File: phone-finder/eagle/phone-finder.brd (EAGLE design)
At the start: 50 x 50 mm, 45 parts, among them J1 MICRO USB, J2 PHONE-JACK, K1 RELAY, Q1 DTA114EET1G (2x10K), Q2 2N2222, Q3 2N2222, T1 TRANSFORMER, U1 AP2114H-3.3TRG1, U2 NUF2042XV6T1G, U3 LPC11U35FHI33/501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

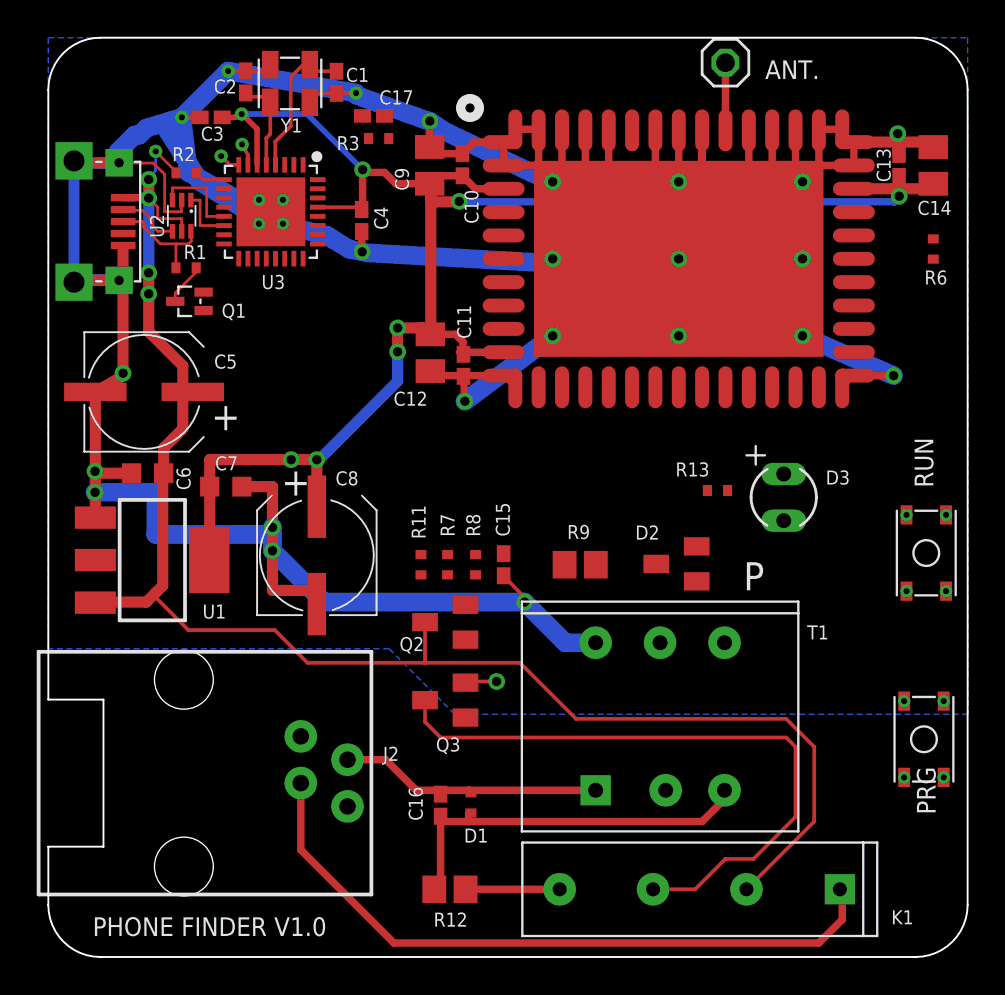
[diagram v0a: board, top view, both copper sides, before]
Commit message: Moved the USB connector 1mm away from the board edge.
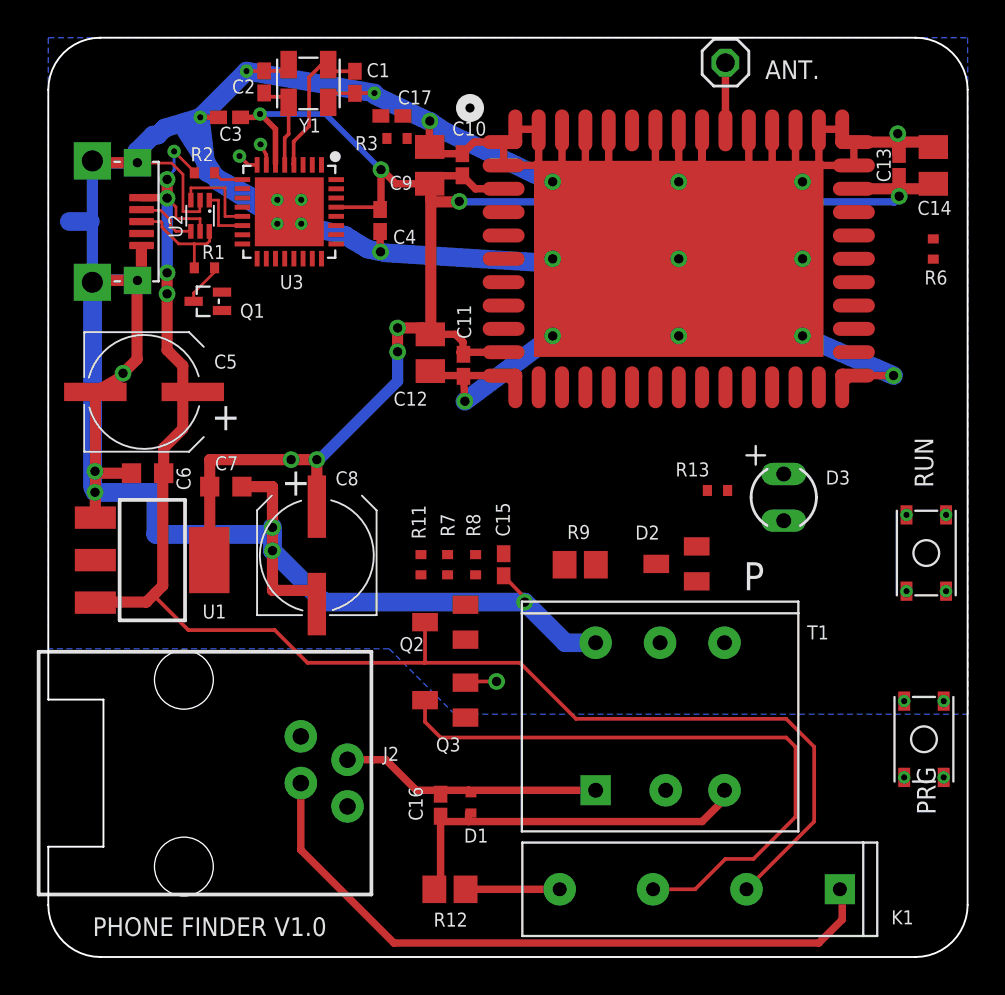
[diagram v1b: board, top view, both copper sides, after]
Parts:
- moved C1 1.00 mm to (16.7, 47.6)
- moved C17 1.00 mm to (18.7, 45.7)
- moved C2 1.00 mm to (11.7, 47.6)
- moved C3 1.00 mm to (9.86, 45.7)
- moved C4 1.00 mm to (18.0, 40.1)
- moved Q1 1.00 mm to (8.67, 35.7)
- moved R1 1.00 mm to (8.49, 37.5)
- moved R2 1.00 mm to (8.49, 42.6)
- moved R3 1.00 mm to (19.0, 44.5)
- moved U2 1.00 mm to (8.25, 40.3)
- moved U3 1.00 mm to (13.1, 40.5)
- moved Y1 1.00 mm to (14.1, 47.5)
- moved J1 1.00 mm to (2.40, 40.0)
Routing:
- net GND: track 419.8 -> 432.9 mm
- net +3V3: track 97.5 -> 96.5 mm

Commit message: Tweaked the PROG button position.
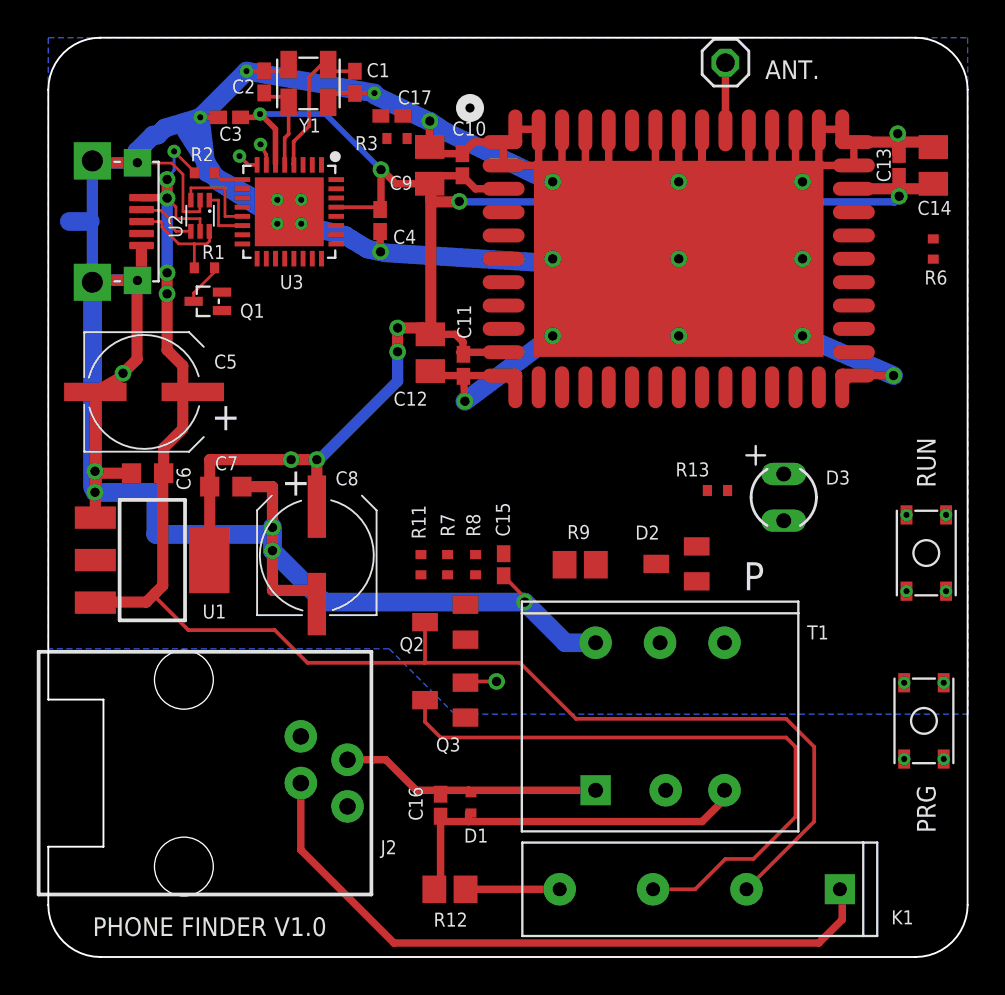
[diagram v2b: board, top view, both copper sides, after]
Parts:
- moved S1 1.00 mm to (47.6, 12.8)
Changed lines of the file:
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@@
 <setting verticaltext="up"/>
 </settings>
-<grid distance="5" unitdist="mil" unit="mil" style="lines" multiple="1" display="no" altdistance="1" altunitdist="mil" altunit="mil"/>
+<grid distance="5" unitdist="mil" unit="mm" style="lines" multiple="1" display="no" altdistance="1" altunitdist="mil" altunit="mil"/>
 <layers>
 <layer number="1" name="Top" color="4" fill="1" visible="yes" active="yes"/>
@@
 <board>
 <plain>
-<text x="48.26" y="7.747" size="1.016" layer="21" font="vector" ratio="10" rot="R90">PRG</text>
-<text x="48.133" y="25.527" size="1.016" layer="21" font="vector" ratio="10" rot="R90">RUN</text>
+<text x="48.26" y="6.747" size="1.016" layer="21" font="vector" ratio="10" rot="R90">PRG</text>
+<text x="48.26" y="25.527" size="1.016" layer="21" font="vector" ratio="10" rot="R90">RUN</text>
 <text x="12.6746" y="25.0952" size="1.524" layer="21" font="vector" ratio="10">+</text>
 <wire x1="50" y1="2.828425" x2="50" y2="47.171575" width="0.1016" layer="20"/>
@@
 <elements>
 <element name="J1" library="phone-finder" package="USB-MICRO" value="MICRO USB" x="2.397" y="40" smashed="yes" rot="R270"/>
-<element name="S1" library="phone-finder" package="PUSH_BUTTON" value="PUSH-BUTTON" x="47.625" y="11.843" smashed="yes" rot="R270"/>
+<element name="S1" library="phone-finder" package="PUSH_BUTTON" value="PUSH-BUTTON" x="47.625" y="12.843" smashed="yes" rot="R270"/>
 <element name="C7" library="phone-finder" package="C0603K" value="1u" x="9.656" y="25.583" smashed="yes">
 <attribute name="NAME" x="10.321" y="27.234" size="0.762" layer="25" font="vector" ratio="10" rot="R180"/>
@@
 <attribute name="MF" value="" x="7.374" y="10" size="1.778" layer="27" rot="R270" display="off"/>
 <attribute name="OC_FARNELL" value="unknown" x="7.374" y="10" size="1.778" layer="27" rot="R270" display="off"/>
-<attribute name="NAME" x="18.202" y="10.668" size="0.762" layer="25" font="vector" ratio="10"/>
+<attribute name="NAME" x="18.075" y="5.588" size="0.762" layer="25" font="vector" ratio="10"/>
 </element>
 <element name="D3" library="phone-finder" package="LED" value="LED" x="40" y="25" smashed="yes" rot="R270">
@@
 <contactref element="S1" pad="B2"/>
 <contactref element="S1" pad="B2P"/>
-<wire x1="46.55" y1="9.768" x2="46.55" y2="13.918" width="0" layer="19" extent="1-1"/>
-<wire x1="33.0668" y1="21.382" x2="46.55" y2="13.918" width="0" layer="19" extent="1-1"/>
+<wire x1="46.55" y1="10.768" x2="46.55" y2="14.918" width="0" layer="19" extent="1-1"/>
+<wire x1="33.0668" y1="21.382" x2="46.55" y2="14.918" width="0" layer="19" extent="1-1"/>
 </signal>
 <signal name="WIFI_RESET">
@@
 <wire x1="46.677" y1="24.046" x2="45.974" y2="31.623" width="0" layer="19" extent="1-1"/>
 <wire x1="46.677" y1="19.896" x2="46.677" y2="24.046" width="0" layer="19" extent="1-1"/>
-<wire x1="48.7" y1="13.918" x2="46.677" y2="19.896" width="0" layer="19" extent="1-1"/>
-<wire x1="48.7" y1="9.768" x2="48.7" y2="13.918" width="0" layer="19" extent="1-1"/>
+<wire x1="48.7" y1="14.918" x2="46.677" y2="19.896" width="0" layer="19" extent="1-1"/>
+<wire x1="48.7" y1="10.768" x2="48.7" y2="14.918" width="0" layer="19" extent="1-1"/>
 <wire x1="40" y1="23.73" x2="46.677" y2="24.046" width="0" layer="19" extent="1-1"/>
 <wire x1="4.826" y1="36.703" x2="4.826" y2="32.512" width="0.6096" layer="1"/>

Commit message: Performed final auto routing.
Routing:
- net LED: track 1.20 -> 76.4 mm, vias 1 -> 5
- net WIFI_WAKE: track 0.00 -> 62.8 mm, vias 0 -> 4
- net ISP_EN: track 0.00 -> 62.0 mm, vias 0 -> 4
- net WIFI_FACTORY: track 0.00 -> 60.4 mm, vias 0 -> 2
- net RESET: track 0.00 -> 57.7 mm, vias 0 -> 4
- net WIFI_RESET: track 0.00 -> 57.6 mm, vias 0 -> 2
- net WIFI_IRQ: track 1.28 -> 48.6 mm, vias 1 -> 4
- net WIFI_RX: track 0.00 -> 38.8 mm, vias 0 -> 4
- net WIFI_TX: track 0.00 -> 31.9 mm, vias 0 -> 2
- net WIFI_CTS: track 0.00 -> 29.3 mm, vias 0 -> 4
- net WIFI_RTS: track 0.00 -> 28.4 mm, vias 0 -> 4
- net DTMF2: track 0.00 -> 24.9 mm, vias 0 -> 2
- net DTMF1: track 0.00 -> 22.3 mm, vias 0 -> 2
- net N$16: track 0.00 -> 21.0 mm
- net HOOK: track 0.00 -> 18.7 mm
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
